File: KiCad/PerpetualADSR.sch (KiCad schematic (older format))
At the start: 35 parts

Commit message: trigger generated from gate
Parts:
- removed U?: OPAMP, symbol Device:Opamp_Quad_Generic
- added C3: C_Small, symbol Device:C_Small
- added D1, D3: 5.1v, symbol Device:D_Zener_Small
- added D2: D, symbol Device:D_Small
- added R1, R3, R4, R5, R6: 100k, symbol Device:R_Small
- added R2: 47k, symbol Device:R_Small
- added unit 4 of U1
- J1: renamed from J?; value EXT_CLK -> GATE
- J3: renamed from J?; value EXT_CLK -> TRIG
- gave numbers to parts that had none: 25
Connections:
- net labels added: +12V, +5V, -12V
- net labels removed: !Q
- wire segments 113 -> 172
- no-connect marks 14 -> 7
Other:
- moved on the sheet: C4, J1, J2, J3, J4, R7, R8, R9, RV1, RV4, RV5, RV6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

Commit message: added component names
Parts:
- removed Q1: NPN, symbol Device:Q_NPN_BCE
- removed U1: OPAMP, symbol Device:Opamp_Quad_Generic
- removed U2: 74HC02, symbol 74xx:74HC02
- added C3: 0.1uF, symbol Device:C_Small
- added C4, C5, C6: 1uF, symbol Device:C_Small
- added D4: ZMM5V1, symbol Device:D_Zener_Small
- added Q1: S8050, Package_TO_SOT_THT:TO-92_Inline, symbol Transistor_BJT:S8050
- added U1: LM324, symbol Amplifier_Operational:LM324
- added U2: 4001, symbol 4xxx:4001
- C1, C2: value C_Small -> 0.1uF
- D1, D3: value 5.1v -> ZMM5V1
- D2: value D -> 1N4148
- J1: renamed from J2; value Conn_02x08_Odd_Even -> PWR_Conn
- renumbered C4 to C7, C3 to C8, J1 to J2, J4 to J3, J3 to J4, R7 to R1, R8 to R2, R9 to R3, R1 to R4, R2 to R5, R3 to R6, R4 to R7, R5 to R8, R6 to R9, RV4 to RV2, RV5 to RV3, RV2 to RV4, RV6 to RV5, RV3 to RV6
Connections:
- net labels removed: VCC
- wire segments 172 -> 195
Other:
- moved on the sheet: C1, C2, C7, C8, D1, J1, J2, J3, J4, J5, R1, R10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

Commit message: 6hp version
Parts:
- removed C7: C_Small, symbol Device:C_Small
- removed J2: GATE, symbol Connector:AudioJack2_SwitchT
- removed J3: OUT, symbol Connector:AudioJack2_SwitchT
- removed J4: TRIG, symbol Connector:AudioJack2_SwitchT
- removed J5: EXT_CLK, symbol Connector:AudioJack2_SwitchT
- removed Q1: S8050, Package_TO_SOT_THT:TO-92_Inline, symbol Transistor_BJT:S8050
- removed RV1, RV4: POT, symbol Device:R_POT_Small
- removed SW1: SW_Push_SPDT, symbol Switch:SW_Push_SPDT
- added C7: 10u, Capacitor_Tantalum_SMD:CP_EIA-3216-10_Kemet-I, symbol Device:CP_Small
- added J2, J3, J4, J5: PJ-301M, PJ301M:PJ301M, symbol PJ-301M:PJ-301M
- added Q1: SS8050, SOT-23-3:SOT-23-3, symbol SS8050:SS8050
- added R10: 1k, Resistor_SMD:R_0805_2012Metric, symbol Device:R_Small
- added S1: 1825255-1, 1825255:SW_1825255-1, symbol 1825255-1:1825255-1
- C1, C2, C3, C4, C5, C6: footprint (none) -> Capacitor_SMD:C_0805_2012Metric
- C8: value C_Small -> 10n; footprint (none) -> Capacitor_SMD:C_0805_2012Metric
- D1: renamed from D2; footprint (none) -> Diode_SMD:D_SOD-323F
- D2: renamed from D1; value ZMM5V1 -> ZMM5V6; footprint (none) -> Diode_SMD:D_MiniMELF
- D3, D4: value ZMM5V1 -> ZMM5V6; footprint (none) -> Diode_SMD:D_MiniMELF
- J1: footprint (none) -> Connector_IDC:IDC-Header_2x08_P2.54mm_Vertical
- R1: value R_Small -> 1k; footprint (none) -> Resistor_SMD:R_0805_2012Metric
- R11, R2: value R_Small -> 56k; footprint (none) -> Resistor_SMD:R_0805_2012Metric
- R12: renamed from R10; value R_Small -> 12k; footprint (none) -> Resistor_SMD:R_0805_2012Metric
- R13: renamed from R12; value R_Small -> 56k; footprint (none) -> Resistor_SMD:R_0805_2012Metric
- R14: renamed from R13; footprint (none) -> Resistor_SMD:R_0805_2012Metric
- R3, R4, R5, R6, R8, R9: footprint (none) -> Resistor_SMD:R_0805_2012Metric
- R7: value 100k -> 15k; footprint (none) -> Resistor_SMD:R_0805_2012Metric
- RV1: renamed from RV2; value POT -> 100k; footprint (none) -> Potentiometer_THT:Potentiometer_Alps_RK09L_Single_Vertical
- RV2: renamed from RV3; value POT -> 50k; footprint (none) -> Potentiometer_THT:Potentiometer_Alps_RK09L_Single_Vertical
- RV3: renamed from RV6; value POT -> 10k; footprint (none) -> Potentiometer_THT:Potentiometer_Alps_RK09L_Single_Vertical
- RV4: renamed from RV5; value POT -> 100k; footprint (none) -> Potentiometer_THT:Potentiometer_Alps_RK09L_Single_Vertical
- RV5: renamed from RV7; value POT -> 50k; footprint (none) -> Potentiometer_THT:Potentiometer_Alps_RK09L_Single_Vertical
- U1, U2: footprint (none) -> Package_SO:SOIC-14_3.9x8.7mm_P1.27mm
- U3: footprint (none) -> Package_SO:SOIC-16_3.9x9.9mm_P1.27mm
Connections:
- net labels removed: +12V, -12V
- wire segments 195 -> 198
- no-connect marks 7 -> 11
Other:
- moved on the sheet: D3, D4, R1, R11, R12, R13, R14, R2, R3, R9, RV3

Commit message: started schematic
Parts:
- removed C1, C2, C3: 0.1uF, Capacitor_SMD:C_0805_2012Metric, symbol Device:C_Small
- removed C4, C5, C6: 1uF, Capacitor_SMD:C_0805_2012Metric, symbol Device:C_Small
- removed C7: 10u, Capacitor_Tantalum_SMD:CP_EIA-3216-10_Kemet-I, symbol Device:CP_Small
- removed C8: 10n, Capacitor_SMD:C_0805_2012Metric, symbol Device:C_Small
- removed D1: 1N4148, Diode_SMD:D_SOD-323F, symbol Device:D_Small
- removed D2, D3, D4: ZMM5V6, Diode_SMD:D_MiniMELF, symbol Device:D_Zener_Small
- removed J2, J3, J4, J5: PJ-301M, PJ301M:PJ301M, symbol PJ-301M:PJ-301M
- removed Q1: SS8050, SOT-23-3:SOT-23-3, symbol SS8050:SS8050
- removed R1, R10: 1k, Resistor_SMD:R_0805_2012Metric, symbol Device:R_Small
- removed R11, R13, R2: 56k, Resistor_SMD:R_0805_2012Metric, symbol Device:R_Small
- removed R12: 12k, Resistor_SMD:R_0805_2012Metric, symbol Device:R_Small
- removed R14: 100K, Resistor_SMD:R_0805_2012Metric, symbol Device:R_Small
- removed R3: 10k, Resistor_SMD:R_0805_2012Metric, symbol Device:R_Small
- removed R4, R6, R8, R9: 100k, Resistor_SMD:R_0805_2012Metric, symbol Device:R_Small
- removed R5: 47k, Resistor_SMD:R_0805_2012Metric, symbol Device:R_Small
- removed R7: 15k, Resistor_SMD:R_0805_2012Metric, symbol Device:R_Small
- removed RV1, RV4: 100k, Potentiometer_THT:Potentiometer_Alps_RK09L_Single_Vertical, symbol Device:R_POT_Small
- removed RV2, RV5: 50k, Potentiometer_THT:Potentiometer_Alps_RK09L_Single_Vertical, symbol Device:R_POT_Small
- removed RV3: 10k, Potentiometer_THT:Potentiometer_Alps_RK09L_Single_Vertical, symbol Device:R_POT_Small
- removed S1: 1825255-1, 1825255:SW_1825255-1, symbol 1825255-1:1825255-1
- removed U1: LM324, Package_SO:SOIC-14_3.9x8.7mm_P1.27mm, symbol Amplifier_Operational:LM324
- removed U2: 4001, Package_SO:SOIC-14_3.9x8.7mm_P1.27mm, symbol 4xxx:4001
- removed U3: CD4053B, Package_SO:SOIC-16_3.9x9.9mm_P1.27mm, symbol Analog_Switch:CD4053B
- added C? (x2): 22p, symbol Device:C_Small
- added D? (x2): 5.1V, symbol Device:D_Zener_Small
- added D? (x2): Schottky, symbol Device:D_Schottky_Small
- added D?: LED_RGBC, symbol Device:LED_RGBC
- added J?: OUT, symbol Connector:AudioJack2_SwitchT
- added J?: GATE, symbol Connector:AudioJack2_SwitchT
- added J?: CLOCK, symbol Connector:AudioJack2_SwitchT
- added R?: 220, symbol Device:R_Small
- added R?: 1M, symbol Device:R_Small
- added RV?: ATT_V, symbol Device:R_POT_Small
- added RV?: ATT_T, symbol Device:R_POT_Small
- added RV?: RISE_T, symbol Device:R_POT_Small
- added RV?: RISE_V, symbol Device:R_POT_Small
- added RV?: FALL_T, symbol Device:R_POT_Small
- added RV?: FALL_V, symbol Device:R_POT_Small
- added RV?: REL_T, symbol Device:R_POT_Small
- added RV?: MAX_V, symbol Device:R_POT_Small
- added U?: ATmega328P-PU, Package_DIP:DIP-28_W7.62mm, symbol MCU_Microchip_ATmega:ATmega328P-PU
- added U?: MCP3208, symbol Analog_ADC:MCP3208
- added U?: MCP4901, symbol Analog_DAC:MCP4901
- added Y?: 16MHz, symbol Device:Crystal_Small
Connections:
- net labels removed: ATT_SUS, BUFF, GATE, TRIG, UP_DOWN
- wire segments 198 -> 138
- no-connect marks 11 -> 10
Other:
- note removed: "0"
- note removed: "1"
- moved on the sheet: J1

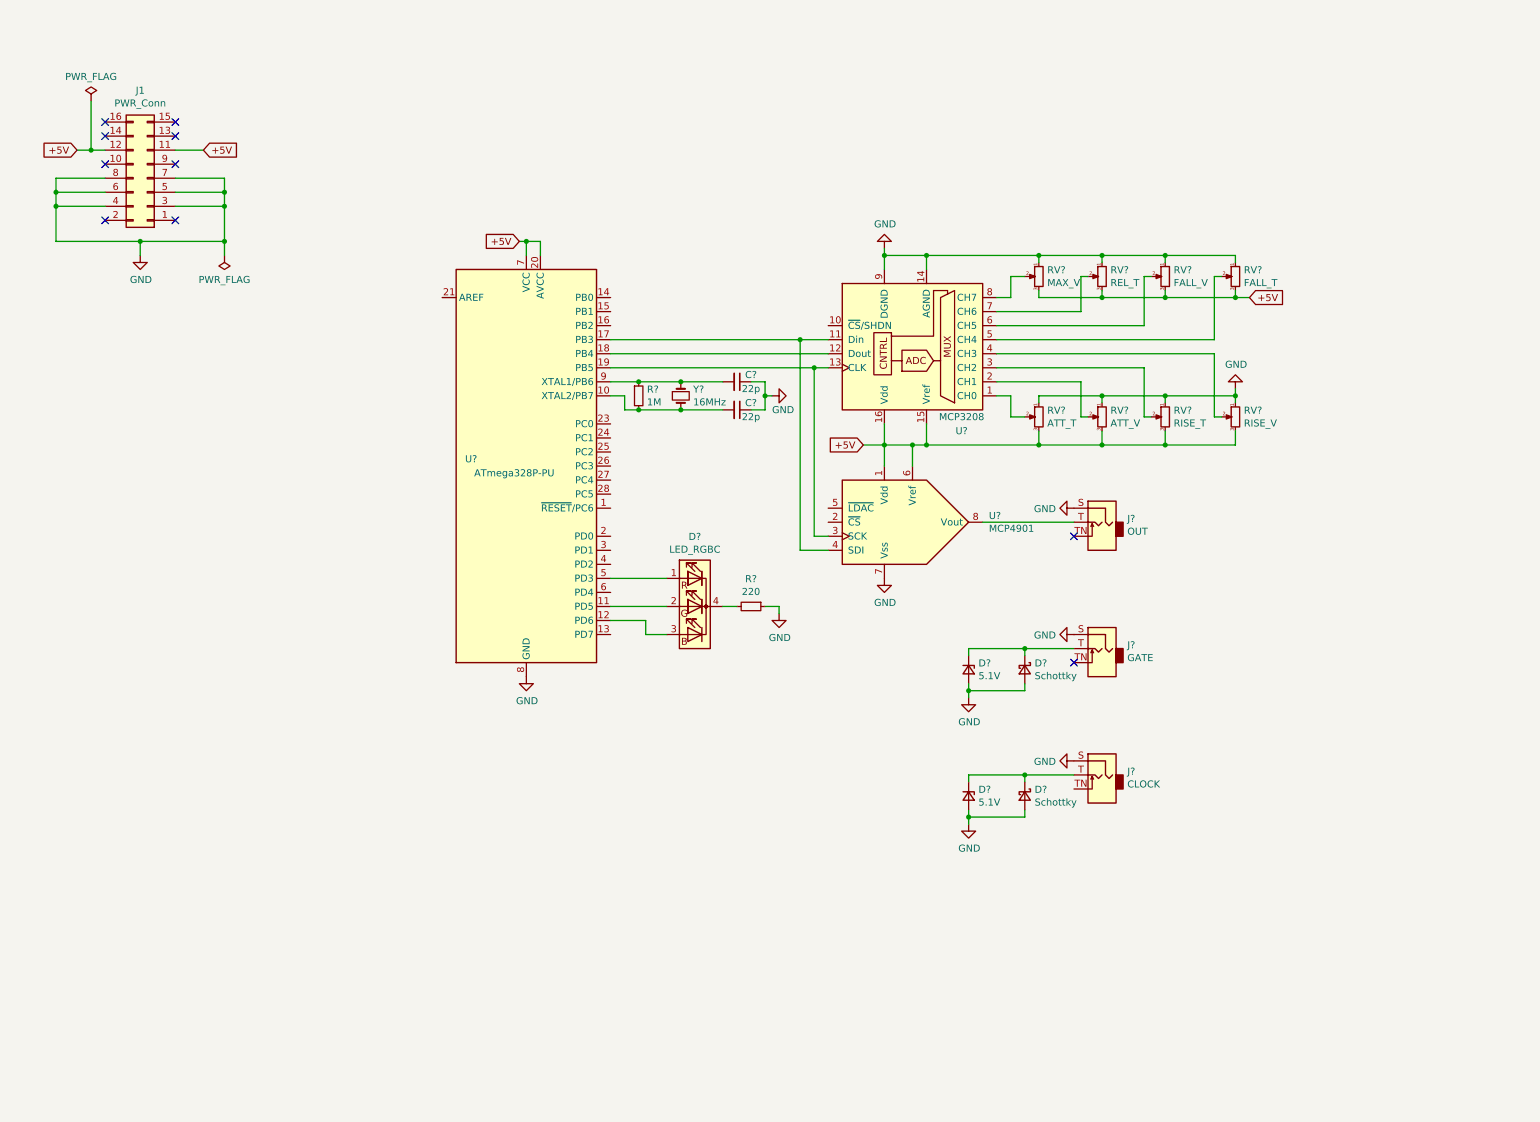
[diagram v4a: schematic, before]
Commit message: added jacks for every pot
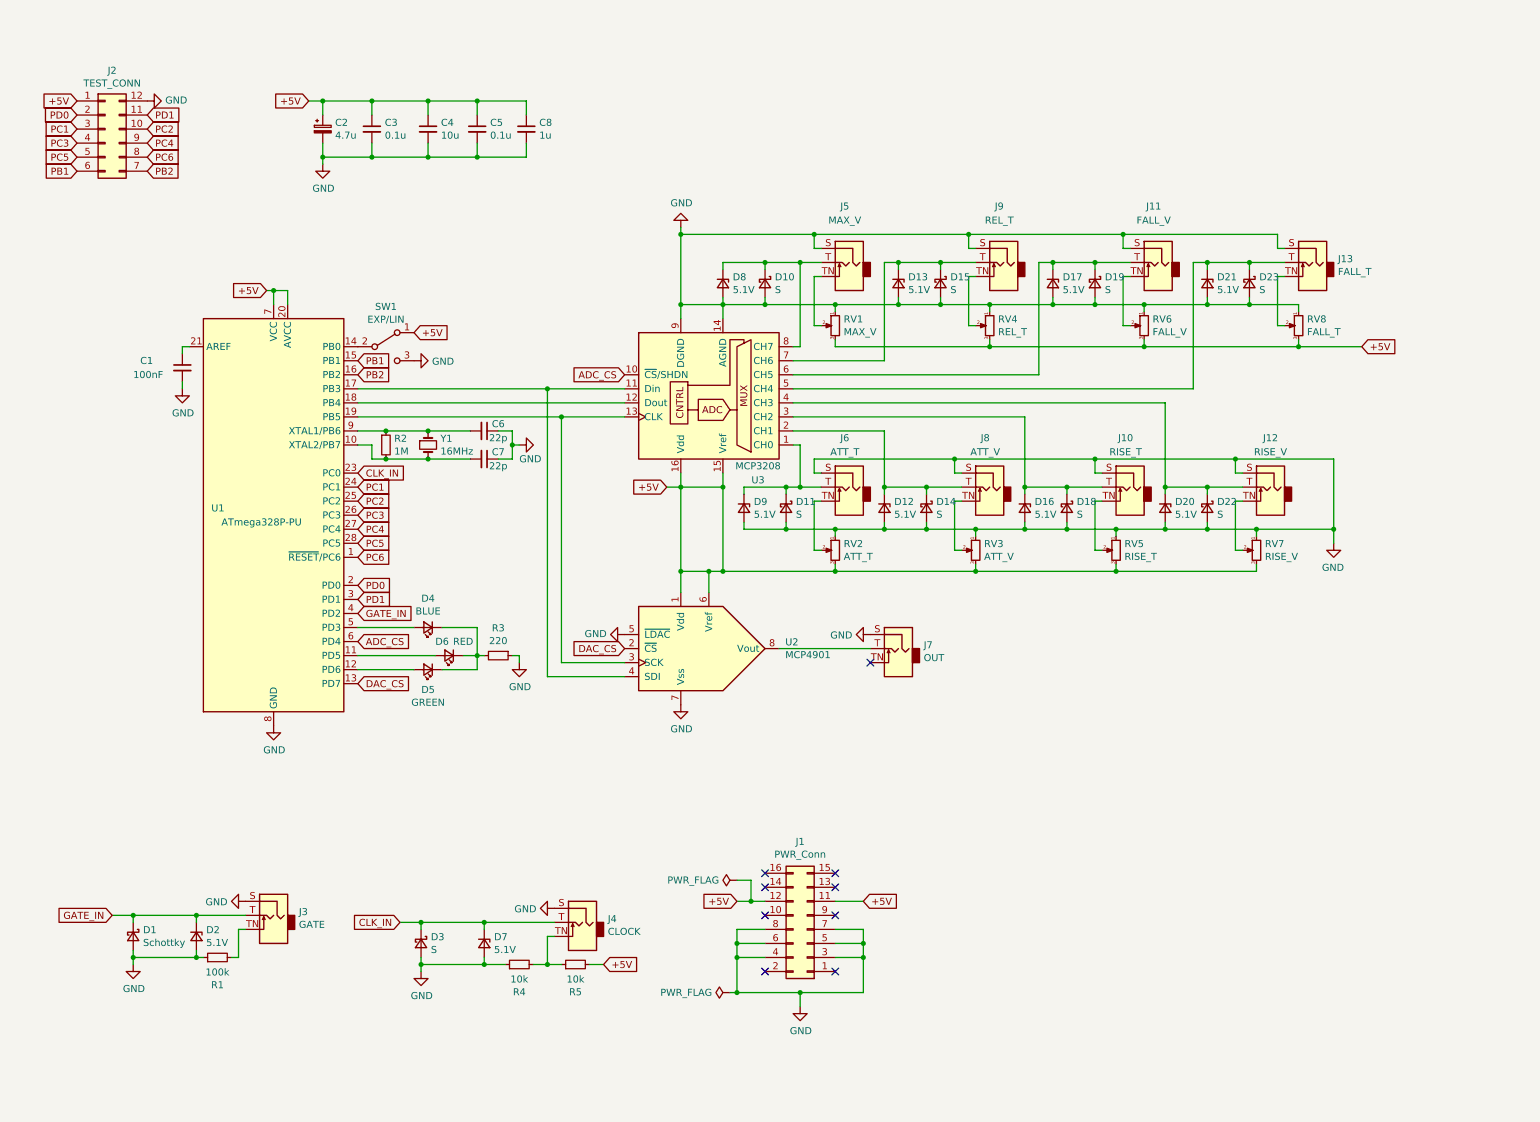
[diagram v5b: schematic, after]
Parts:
- removed D?: LED_RGBC, symbol Device:LED_RGBC
- added C1: 100nF, symbol Device:C_Small
- added C2: 4.7u, symbol Device:CP_Small
- added C3, C5: 0.1u, symbol Device:C_Small
- added C4: 10u, symbol Device:C_Small
- added C8: 1u, symbol Device:C_Small
- added D10, D11, D14, D15, D18, D19, D22, D23: S, symbol Device:D_Schottky_Small
- added D12, D13, D16, D17, D20, D21, D8, D9: 5.1V, symbol Device:D_Zener_Small
- added D4: BLUE, symbol Device:LED_Small
- added D5: GREEN, symbol Device:LED_Small
- added D6: RED, symbol Device:LED_Small
- added J10: RISE_T, symbol Connector:AudioJack2_SwitchT
- added J11: FALL_V, symbol Connector:AudioJack2_SwitchT
- added J12: RISE_V, symbol Connector:AudioJack2_SwitchT
- added J13: FALL_T, symbol Connector:AudioJack2_SwitchT
- added J2: TEST_CONN, symbol Connector_Generic:Conn_02x06_Counter_Clockwise
- added J5: MAX_V, symbol Connector:AudioJack2_SwitchT
- added J6: ATT_T, symbol Connector:AudioJack2_SwitchT
- added J8: ATT_V, symbol Connector:AudioJack2_SwitchT
- added J9: REL_T, symbol Connector:AudioJack2_SwitchT
- added R1: 100k, symbol Device:R_Small
- added R4, R5: 10k, symbol Device:R_Small
- added SW1: EXP/LIN, symbol Switch:SW_SPDT
- D3: renamed from D?; value Schottky -> S
- gave numbers to parts that had none: 22
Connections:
- net +5V: now also C2.1, C3.1, C4.1, C5.1, C8.1, J2.1 (Pin_1), R5.2, SW1.1 (A)
- net GND: now also U2.5 (~LDAC), C1.2, C2.2, C3.2, C4.2, C5.2, C8.2, D10.2 (A), D11.2 (A), D12.2 (A), D13.2 (A), D14.2 (A), D15.2 (A), D16.2 (A), D17.2 (A), D18.2 (A), D19.2 (A), D20.2 (A), D21.2 (A), D22.2 (A), D23.2 (A), D8.2 (A), D9.2 (A), J10.S, J11.S, J12.S, J13.S, J2.12 (Pin_12), J5.S, J6.S, J8.S, J9.S, R1.1, R4.1, SW1.3 (C)
- net PC6: now reaches U1.1 (~RESET~/PC6)
- net PC6: now also J2.8 (Pin_8)
- net at U1.11 (PD5): now also D6.2 (A)
- net at U1.12 (PD6): now also D5.2 (A)
- net DAC_CS: now reaches U1.13 (PD7)
- net DAC_CS: now also U2.2 (~CS)
- net at U1.14 (PB0): now also SW1.2 (B)
- net PB1: now reaches U1.15 (PB1)
- net PB1: now also J2.6 (Pin_6)
- net PB2: now reaches U1.16 (PB2)
- net PB2: now also J2.7 (Pin_7)
- net PD0: now reaches U1.2 (PD0)
- net PD0: now also J2.2 (Pin_2)
- net at U1.21 (AREF): now also C1.1
- net CLK_IN: now reaches U1.23 (PC0)
- net CLK_IN: now also D3.1 (K), D7.1 (K), J4.T
- net PC1: now reaches U1.24 (PC1)
- net PC1: now also J2.3 (Pin_3)
- net PC2: now reaches U1.25 (PC2)
- net PC2: now also J2.10 (Pin_10)
- net PC3: now reaches U1.26 (PC3)
- net PC3: now also J2.4 (Pin_4)
- net PC4: now reaches U1.27 (PC4)
- net PC4: now also J2.9 (Pin_9)
- net PC5: now reaches U1.28 (PC5)
- net PC5: now also J2.5 (Pin_5)
- net PD1: now reaches U1.3 (PD1)
- net PD1: now also J2.11 (Pin_11)
- net GATE_IN: now reaches U1.4 (PD2)
- net GATE_IN: now also D1.1 (K), D2.1 (K), J3.T
- net at U1.5 (PD3): now also D4.2 (A)
- net ADC_CS: now reaches U1.6 (PD4)
- net ADC_CS: now also U3.10 (~CS~/SHDN)
- net at U3.1 (CH0): now also D11.1 (K), D9.1 (K), J6.T; no longer RV2.2
- net at U3.2 (CH1): now also D12.1 (K), D14.1 (K), J8.T; no longer RV3.2
- net at U3.3 (CH2): now also D16.1 (K), D18.1 (K), J10.T; no longer RV5.2
- net at U3.4 (CH3): now also D20.1 (K), D22.1 (K), J12.T; no longer RV7.2
- net at U3.5 (CH4): now also D21.1 (K), D23.1 (K), J13.T; no longer RV8.2
- net at U3.6 (CH5): now also D17.1 (K), D19.1 (K), J11.T; no longer RV6.2
- net at U3.7 (CH6): now also D13.1 (K), D15.1 (K), J9.T; no longer RV4.2
- net at U3.8 (CH7): now also D10.1 (K), D8.1 (K), J5.T; no longer RV1.2
- net at J3.TN: now also R1.2
- net at J4.TN: now also R4.2, R5.1
- net at R3.2: now also D4.1 (K), D5.1 (K), D6.1 (K)
- new net: J8.TN, RV3.2
- new net: J6.TN, RV2.2
- new net: J10.TN, RV5.2
- new net: J12.TN, RV7.2
- new net: J13.TN, RV8.2
- new net: J11.TN, RV6.2
- new net: J9.TN, RV4.2
- new net: J5.TN, RV1.2
- no-connect marks 10 -> 9
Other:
- moved on the sheet: C6, C7, D1, D2, D3, D7, J1, J3, J4, J7, R2, R3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

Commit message: schematics done
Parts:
- removed U2: MCP4901, symbol Analog_DAC:MCP4901
- added U2: MCP4921, Package_DIP:DIP-8_W7.62mm, symbol Analog_DAC:MCP4921
- C1: value 100nF -> 0.1u; footprint (none) -> Capacitor_THT:C_Disc_D5.0mm_W2.5mm_P5.00mm
- C2, C8: footprint (none) -> Capacitor_THT:C_Disc_D5.0mm_W2.5mm_P2.50mm
- C3, C4, C5, C6, C7: footprint (none) -> Capacitor_THT:C_Disc_D5.0mm_W2.5mm_P5.00mm
- D1, D10, D11, D14, D15, D18, D19, D22, D23, D3: footprint (none) -> Diode_THT:D_DO-34_SOD68_P7.62mm_Horizontal
- D12, D13, D16, D17, D2, D20, D21, D7, D8, D9: footprint (none) -> Diode_THT:D_DO-35_SOD27_P7.62mm_Horizontal
- D4, D5, D6: footprint (none) -> LED_THT:LED_D5.0mm
- J10, J11, J12, J13, J3, J4, J5, J6, J7, J8, J9: footprint (none) -> PerpetualADSR:PJ301M
- J2: footprint (none) -> Connector_PinHeader_2.54mm:PinHeader_2x06_P2.54mm_Vertical
- R1, R2, R3, R4, R5: footprint (none) -> Resistor_THT:R_Axial_DIN0207_L6.3mm_D2.5mm_P7.62mm_Horizontal
- RV1, RV2, RV3, RV4, RV5, RV6, RV7, RV8: footprint (none) -> PerpetualADSR:Potentiometer_Alps_RK09L_Single_Vertical
- SW1: footprint (none) -> PerpetualADSR:SLIDE_SW_OS102011MS2QN1
- U3: footprint (none) -> Package_DIP:DIP-14_W7.62mm
- Y1: footprint (none) -> Crystal:Crystal_HC49-4H_Vertical
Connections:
- net +5V: now also U2.1 (Vdd), U2.6 (Vref)
- net DAC_CS: now also U2.2 (~CS)
- net GND: now also U2.5 (~LDAC), U2.7 (Vss)
- net at U1.17 (PB3), U3.11 (Din): now also U2.4 (SDI)
- net at U1.19 (PB5), U3.13 (CLK): now also U2.3 (SCK)
- net at J7.T: now also U2.8 (Vout)

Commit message: starting PCB
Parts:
- removed D10, D11, D14, D15, D18, D19, D22, D23: S, Diode_THT:D_DO-34_SOD68_P7.62mm_Horizontal, symbol Device:D_Schottky_Small
- removed D12, D13, D16, D17, D20, D21, D8, D9: 5.1V, Diode_THT:D_DO-35_SOD27_P7.62mm_Horizontal, symbol Device:D_Zener_Small
- removed J10: RISE_T, PerpetualADSR:PJ301M, symbol Connector:AudioJack2_SwitchT
- removed J11: FALL_V, PerpetualADSR:PJ301M, symbol Connector:AudioJack2_SwitchT
- removed J12: RISE_V, PerpetualADSR:PJ301M, symbol Connector:AudioJack2_SwitchT
- removed J13: FALL_T, PerpetualADSR:PJ301M, symbol Connector:AudioJack2_SwitchT
- removed J5: MAX_V, PerpetualADSR:PJ301M, symbol Connector:AudioJack2_SwitchT
- removed J6: ATT_T, PerpetualADSR:PJ301M, symbol Connector:AudioJack2_SwitchT
- removed J8: ATT_V, PerpetualADSR:PJ301M, symbol Connector:AudioJack2_SwitchT
- removed J9: REL_T, PerpetualADSR:PJ301M, symbol Connector:AudioJack2_SwitchT
- U3: footprint Package_DIP:DIP-14_W7.62mm -> Package_DIP:DIP-16_W7.62mm
- renumbered C8 to C6, C6 to C7, C7 to C8, D7 to D6, D6 to D7, J2 to J1, J3 to J2, J4 to J3, J1 to J4, J7 to J5, R4 to R3, R3 to R4, RV4 to RV3, RV3 to RV4, RV6 to RV5, RV5 to RV6, RV8 to RV7, RV7 to RV8
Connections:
- net at U3.1 (CH0): now also RV2.2
- net at U3.2 (CH1): now also RV4.2
- net at U3.3 (CH2): now also RV6.2
- net at U3.4 (CH3): now also RV8.2
- net at U3.5 (CH4): now also RV7.2
- net at U3.6 (CH5): now also RV5.2
- net at U3.7 (CH6): now also RV3.2
- net at U3.8 (CH7): now also RV1.2
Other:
- moved on the sheet: C1, C7, C8, D4, D5, D7, J5, R2, R4, RV1, RV2, RV3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
